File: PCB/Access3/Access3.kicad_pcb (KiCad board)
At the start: 2 copper layers, 50 x 26.5 mm, 71 parts, among them J1 USB-C, J2 RFID, J3 INPUTS, J4 Shelly, J5 POWER, J6 DOOR, Q1 NX7002AK, Q2 PMF250XNEX, SW1 ESE13V01D, U1 ESP32-PICO-MINI-02, U2 FT231XQ, U3 G3VM-41GR8, U4 LMR16006XDDCR, U5 LMR16006XDDCR, U6 AA, U7 QR

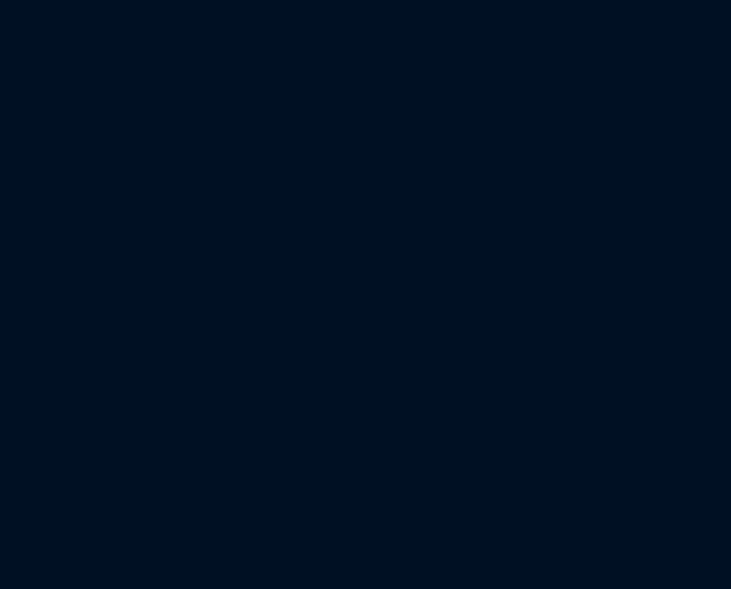
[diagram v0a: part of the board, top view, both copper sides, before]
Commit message: Started new board with two relay outputs
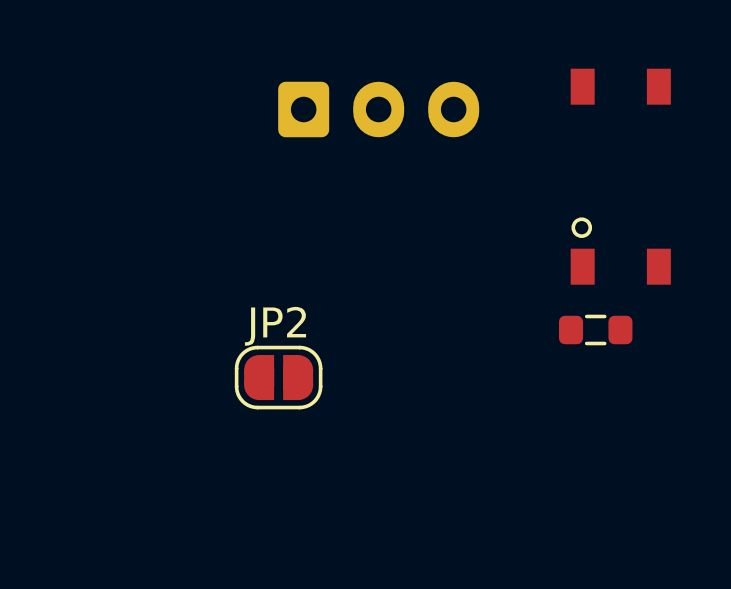
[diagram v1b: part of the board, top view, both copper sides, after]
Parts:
- added J7: DOOR1, RevK:Molex_MiniSPOX_H3RA, F.Cu at (164.1, 67.6)
- added JP2: 12V, Jumper:SolderJumper-2_P1.3mm_Open_RoundedPad1.0x1.5mm, F.Cu at (160.8, 76.5)
- added R25: 1K, RevK:R_0603, F.Cu at (171.3, 75.0)
- added U8: G3VM-41GR8, RevK:Special-SOP-4-3.7x4.55, F.Cu at (172.2, 69.8)
- J6: value DOOR -> DOOR2
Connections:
- R16 pad 2: OUT1 -> RELAY2
- U1 pad 17: unconnected-(U1-Pad17) -> RELAY2
- U1 pad 18: OUT1 -> RELAY1
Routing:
- net RELAY2: track 0.00 -> 32.2 mm, vias 0 -> 2
- net OUT1: track 32.2 -> 0.00 mm, vias 2 -> 0
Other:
- board text added: "Solar System Access3"
- board text removed: "Solar System Access2"

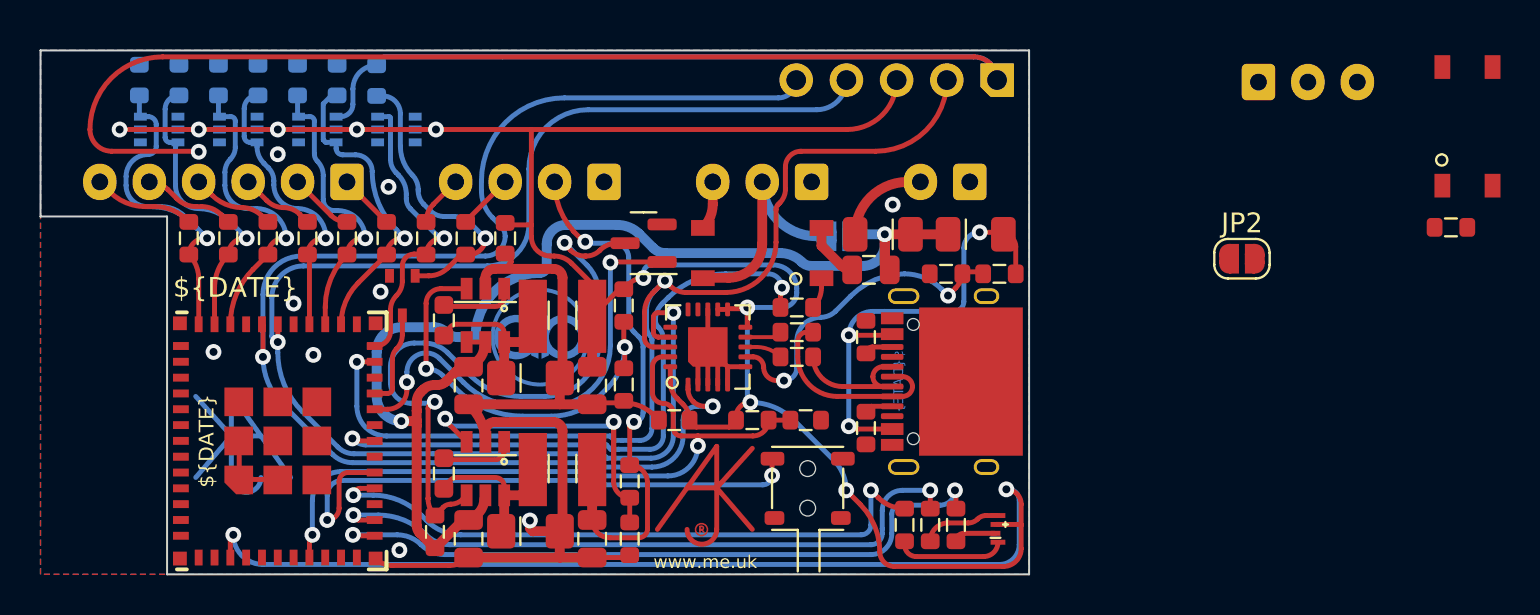
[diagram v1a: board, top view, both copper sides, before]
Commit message: New dual output board
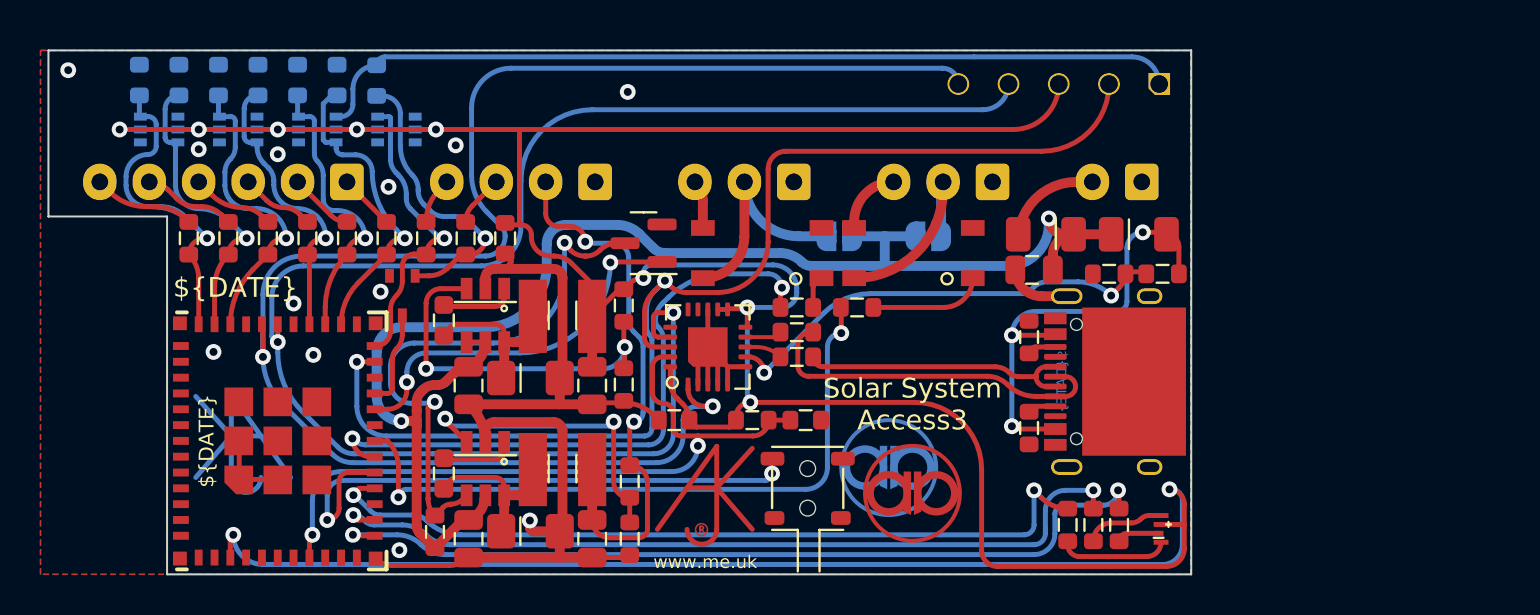
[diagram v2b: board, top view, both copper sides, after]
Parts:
- added U9: AA, RevK:AA, F.Cu at (144.1, 88.4)
- JP2: moved to B.Cu
- moved R25 30.3 mm to (141.3, 79.0), turned to 180 degrees
- moved U8 28.7 mm to (144.2, 76.2), turned to 90 degrees
- moved J7 19.1 mm to (145.7, 72.7), turned to 180 degrees
- moved U6 18.8 mm to (142.9, 87.1)
- moved JP2 15.9 mm to (144.9, 75.4)
- moved J5 8.70 mm to (154.4, 72.7)
- moved C17 8.25 mm to (150.2, 77.1)
- moved D5 8.25 mm to (156.6, 90.2)
- moved D8 8.25 mm to (155.6, 75.3)
- moved D9 8.25 mm to (150.8, 75.3)
- moved J1 8.25 mm to (153.8, 82.8)
- moved R17 8.25 mm to (154.6, 90.0)
- moved R18 8.25 mm to (151.9, 90.0)
- moved R19 8.25 mm to (153.2, 90.0)
- moved R2 8.25 mm to (156.8, 77.3)
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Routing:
- net GND: track 122.2 -> 75.0 mm, vias 10 -> 12
- net RELAY1: track 0.00 -> 34.5 mm, vias 0 -> 2
- net +3.3V: track 158.8 -> 182.6 mm, vias 11 -> 10
- net O: track 70.0 -> 81.1 mm
- net +12V: track 59.4 -> 69.4 mm
- net Net-(J7-Pad2): track 0.00 -> 9.54 mm
- net G: track 32.0 -> 40.3 mm
- net B: track 33.7 -> 42.0 mm
- net R: track 35.0 -> 43.2 mm
- net BOOT: track 53.6 -> 61.7 mm
- net Net-(J1-PadA7): track 10.2 -> 18.2 mm
- net I: track 72.7 -> 80.3 mm
- net Net-(J1-PadA6): track 6.80 -> 13.7 mm
- net Net-(Q1-Pad3): track 34.2 -> 27.5 mm
- net Net-(R2-Pad2): track 16.7 -> 23.1 mm
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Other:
- board size 50 x 26.5 mm -> 57.8 x 26.5 mm
- board text added: "Lock Relays"

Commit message: New cases
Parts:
- moved U6 2.48 mm to (144.5, 85.2)
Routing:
- net GND: track 75.0 -> 76.7 mm, vias 12 -> 14
- net SHDN: track 18.9 -> 20.5 mm
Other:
- board text added: "1"
- board text added: "2"
- board text added: "DC"
- board text added: "GPIO 1-6"
- board text removed: "Inputs 1-6"
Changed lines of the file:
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@@
   (footprint "RevK:D_1206_" (layer "F.Cu")
     (at 124.78 82.57)
-    (property "JLCPCB Rotation Offset" "180")
+    (property "JLCPCB Rotation Offset" "0")
     (property "LCSC Part #" "C143805")
     (property "Manufacturer" "Bourns")
@@
   (footprint "RevK:D_1206_" (layer "F.Cu")
     (at 124.77 90.31)
-    (property "JLCPCB Rotation Offset" "180")
+    (property "JLCPCB Rotation Offset" "0")
     (property "LCSC Part #" "C143805")
     (property "Manufacturer" "Bourns")
@@
     (descr "SOT-323, SC-70")
     (tags "SOT-323 SC-70")
-    (property "JLCPCB Rotation Offset" "180")
+    (property "JLCPCB Rotation Offset" "0")
     (property "LCSC Part #" "C504047")
     (property "Part No" "PMF250XNEX")
@@
   )
   (footprint "RevK:AA" (layer "B.Cu")
-    (at 142.9 87.1 180)
+    (at 144.5 85.2 180)
     (property "Note" "Non part, PCB printed")
     (property "Sheetfile" "Access3.kicad_sch")
@@
     )
   )
-  (gr_line (start 135.6 71.1) (end 135.6 70.5) (layer "B.SilkS") (width 0.15))
-  (gr_line (start 133.1 70.5) (end 135.6 70.5) (layer "B.SilkS") (width 0.15))
-  (gr_line (start 133.1 70.5) (end 133.1 71.1) (layer "B.SilkS") (width 0.15))
+  (gr_line (start 142.7 76.9) (end 153.2 76.9) (layer "B.SilkS") (width 0.12))
+  (gr_line (start 135 70.4) (end 133.8 70.1) (layer "B.SilkS") (width 0.15))
+  (gr_line (start 145 70.4) (end 143.8 70.1) (layer "B.SilkS") (width 0.15))
   (gr_line (start 143.1 70.4) (end 143.1 71) (layer "B.SilkS") (width 0.15))
-  (gr_line (start 143.1 70.4) (end 145.6 70.4) (layer "B.SilkS") (width 0.15))
+  (gr_line (start 135.6 71) (end 135.6 70.4) (layer "B.SilkS") (width 0.15))
+  (gr_line (start 133.1 70.4) (end 133.1 71) (layer "B.SilkS") (width 0.15))
+  (gr_line (start 143.1 70.4) (end 143.7 70.4) (layer "B.SilkS") (width 0.15))
+  (gr_line (start 135 70.4) (end 135.6 70.4) (layer "B.SilkS") (width 0.15))
   (gr_line (start 145.7 73.7) (end 145.7 74.2) (layer "B.SilkS") (width 0.12))
+  (gr_line (start 145 70.4) (end 145.6 70.4) (layer "B.SilkS") (width 0.15))
   (gr_line (start 135.6 73.7) (end 135.6 75.4) (layer "B.SilkS") (width 0.12))
+  (gr_line (start 133.1 70.4) (end 133.7 70.4) (layer "B.SilkS") (width 0.15))
+  (gr_line (start 142.7 76.3) (end 142.7 76.9) (layer "B.SilkS") (width 0.12))
   (gr_line (start 138.8 75.4) (end 135.6 75.4) (layer "B.SilkS") (width 0.12))
+  (gr_line (start 153.2 76.9) (end 153.2 74.1) (layer "B.SilkS") (width 0.12))
   (gr_line (start 145.6 71) (end 145.6 70.4) (layer "B.SilkS") (width 0.15))
   (gr_line (start 100.4 66) (end 158.2 66) (layer "Edge.Cuts") (width 0.1))
@@
     (effects (font (size 0.8 0.8) (thickness 0.1)) (justify mirror))
   )
-  (gr_text "Power" (at 153.9 74.575) (layer "B.SilkS")
-    (effects (font (size 0.8 0.8) (thickness 0.1)) (justify mirror))
-  )
   (gr_text "Solar System\nAccess3" (at 123.5 87.4) (layer "B.SilkS")
     (effects (font (size 1 1) (thickness 0.15)) (justify mirror))
   )
+  (gr_text "DC" (at 154.4 74.6) (layer "B.SilkS")
+    (effects (font (size 0.8 0.8) (thickness 0.1)) (justify mirror))
+  )
+  (gr_text "1" (at 144.4 71.35) (layer "B.SilkS")
+    (effects (font (size 0.8 0.8) (thickness 0.1)) (justify mirror))
+  )
+  (gr_text "2" (at 134.35 71.35) (layer "B.SilkS")
+    (effects (font (size 0.8 0.8) (thickness 0.1)) (justify mirror))
+  )
   (gr_text "⏚" (at 148.1 70.4 180) (layer "B.SilkS")
     (effects (font (size 1 1) (thickness 0.15)) (justify mirror))
@@
     (effects (font (size 1 1) (thickness 0.15)) (justify mirror))
   )
-  (gr_text "Inputs 1-6" (at 101 70 90) (layer "B.SilkS")
+  (gr_text "GPIO 1-6" (at 110.5 74.4) (layer "B.SilkS")
     (effects (font (size 0.8 0.8) (thickness 0.1)) (justify mirror))
   )
@@
   (segment (start 133.75 82.9) (end 133.75 81) (width 0.25) (layer "F.Cu") (net 3))
   (segment (start 110.05 87.7) (end 110.05 85.75) (width 0.25) (layer "F.Cu") (net 3))
+  (segment (start 125.03 82.57) (end 124.7 82.9) (width 0.5) (layer "F.Cu") (net 3))
   (segment (start 133.25 82.9) (end 133.25 81.5) (width 0.25) (layer "F.Cu") (net 3))
   (segment (start 110.05 87.7) (end 112 87.7) (width 0.25) (layer "F.Cu") (net 3))
   (segment (start 133.75 79.1) (end 133.75 81) (width 0.25) (layer "F.Cu") (net 3))
   (segment (start 134.75 82.9) (end 134.75 82) (width 0.25) (layer "F.Cu") (net 3))
+  (segment (start 126.2625 82.57) (end 125.03 82.57) (width 0.5) (layer "F.Cu") (net 3))
   (segment (start 123.8 76.375) (end 123.8 76.7) (width 0.25) (layer "F.Cu") (net 3))
   (via (at 108.75 81.25) (size 0.8) (drill 0.4) (layers "F.Cu" "B.Cu") (free) (net 3))
@@
   (via (at 117.2 78.2) (size 0.8) (drill 0.4) (layers "F.Cu" "B.Cu") (free) (net 3))
   (via (at 112 71.25) (size 0.8) (drill 0.4) (layers "F.Cu" "B.Cu") (net 3))
+  (via (at 124.7 82.9) (size 0.8) (drill 0.4) (layers "F.Cu" "B.Cu") (net 3))
   (via (at 112.8 78.8) (size 0.8) (drill 0.4) (layers "F.Cu" "B.Cu") (free) (net 3))
   (via (at 124.75 89.7755) (size 0.8) (drill 0.4) (layers "F.Cu" "B.Cu") (net 3))
-  (via (at 121 70.8) (size 0.8) (drill 0.4) (layers "F.Cu" "B.Cu") (free) (net 3))
+  (via (at 126.4 80.3) (size 0.8) (drill 0.4) (layers "F.Cu" "B.Cu") (net 3))
+  (via (at 121 71.1) (size 0.8) (drill 0.4) (layers "F.Cu" "B.Cu") (free) (net 3))
   (arc (start 120.684315 92.05) (mid 121.20694 91.946043) (end 121.65 91.65) (width 0.25) (layer "F.Cu") (net 3))
   (arc (start 123.8 76.7) (mid 123.770711 76.770711) (end 123.7 76.8) (width 0.25) (layer "F.Cu") (net 3))
@@
   (via (at 118.529927 82.779927) (size 0.8) (drill 0.4) (layers "F.Cu" "B.Cu") (net 10))
   (arc (start 118.529927 83.170073) (mid 118.242913 83.862986) (end 117.55 84.15) (width 0.25) (layer "F.Cu") (net 10))
-  (segment (start 119.5 81.3) (end 124.249198 81.3) (width 0.25) (layer "B.Cu") (net 10))
-  (segment (start 118.529927 82.270073) (end 118.529927 82.779927) (width 0.25) (layer "B.Cu") (net 10))
-  (arc (start 124.249198 81.3) (mid 127.483335 79.960376) (end 128.822959 76.726239) (width 0.25) (layer "B.Cu") (net 10))
-  (arc (start 119.5 81.3) (mid 118.814055 81.584128) (end 118.529927 82.270073) (width 0.25) (layer "B.Cu") (net 10))
+  (segment (start 118.529927 82.779927) (end 118.529927 82.270073) (width 0.25) (layer "B.Cu") (net 10))
+  (segment (start 128.822959 76.726239) (end 128.822959 80.077041) (width 0.25) (layer "B.Cu") (net 10))
+  (segment (start 119.5 81.3) (end 127.6 81.3) (width 0.25) (layer "B.Cu") (net 10))
+  (arc (start 118.529927 82.270073) (mid 118.814055 81.584128) (end 119.5 81.3) (width 0.25) (layer "B.Cu") (net 10))
+  (arc (start 128.822959 80.077041) (mid 128.464763 80.941804) (end 127.6 81.3) (width 0.25) (layer "B.Cu") (net 10))
   (segment (start 111.25 81.5) (end 111.25 79.9) (width 0.25) (layer "F.Cu") (net 11))
   (segment (start 132.75 83.146447) (end 132.75 82.9375) (width 0.25) (layer "F.Cu") (net 11))

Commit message: PSTM connectors
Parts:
- J2: footprint RevK:Molex_MiniSPOX_H4RA -> RevK:PTSM-HH-4-RA
- J3: footprint RevK:Molex_MiniSPOX_H6RA -> RevK:PTSM-HH-6-RA
- J5: footprint RevK:Molex_MiniSPOX_H2RA -> RevK:PTSM-HH-2-RA
- J6, J7: footprint RevK:Molex_MiniSPOX_H3RA -> RevK:PTSM-HH-3-RA
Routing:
- net IO6: track 18.8 -> 16.2 mm
- net Net-(J3-Pad6): track 4.22 -> 5.08 mm
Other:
- board size 57.8 x 26.5 mm -> 57.8 x 27 mm

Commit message: White socket
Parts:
- J6: footprint RevK:PTSM-HH-3-RA -> RevK:PTSM-HH-3-RA-W
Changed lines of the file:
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@@
     )
   )
-  (footprint "RevK:PTSM-HH-3-RA" (layer "F.Cu")
+  (footprint "RevK:PTSM-HH-3-RA-W" (layer "F.Cu")
     (at 135.6 72.7 180)
     (property "Sheetfile" "Access3.kicad_sch")
@@
       (effects (font (size 1 1) (thickness 0.15)))
     )
+    (fp_line (start -4.45 7.05) (end -4.45 6.05) (layer "F.SilkS") (width 0.12))
     (fp_line (start -4.45 7.05) (end 4.45 7.05) (layer "F.SilkS") (width 0.12))
-    (fp_line (start -4.45 7.05) (end -4.45 6.05) (layer "F.SilkS") (width 0.12))
     (fp_line (start 4.45 7.05) (end 4.45 6.05) (layer "F.SilkS") (width 0.12))
+    (fp_line (start -4.6 17.75) (end -4.6 -0.3) (layer "F.CrtYd") (width 0.12))
     (fp_line (start -4.6 -0.3) (end 4.6 -0.3) (layer "F.CrtYd") (width 0.12))
+    (fp_line (start 4.6 17.75) (end -4.6 17.75) (layer "F.CrtYd") (width 0.12))
     (fp_line (start 4.6 -0.3) (end 4.6 17.75) (layer "F.CrtYd") (width 0.12))
-    (fp_line (start 4.6 17.75) (end -4.6 17.75) (layer "F.CrtYd") (width 0.12))
-    (fp_line (start -4.6 17.75) (end -4.6 -0.3) (layer "F.CrtYd") (width 0.12))
-    (fp_line (start -4.6 -0.3) (end 4.6 -0.3) (layer "F.Fab") (width 0.12))
     (fp_line (start 4.6 7.2) (end -4.6 7.2) (layer "F.Fab") (width 0.12))
     (fp_line (start -4.6 7.2) (end -4.6 -0.3) (layer "F.Fab") (width 0.12))
     (fp_line (start 4.6 -0.3) (end 4.6 7.2) (layer "F.Fab") (width 0.12))
+    (fp_line (start -4.6 -0.3) (end 4.6 -0.3) (layer "F.Fab") (width 0.12))
     (pad "1" thru_hole roundrect (at -2.5 0 180) (size 1.7 1.85) (drill 0.85) (layers *.Cu *.Mask) (roundrect_rratio 0.25)
       (net 3 "GND") (pinfunction "Pin_1") (pintype "passive"))
@@
     (pad "3" thru_hole oval (at 2.5 0 180) (size 1.7 1.85) (drill 0.85) (layers *.Cu *.Mask)
       (net 41 "Net-(J6-Pad3)") (pinfunction "Pin_3") (pintype "passive"))
-    (model "${REVK_3D}/pxc_1778638_03_PTSM-0-5-3-HH-2-5-THR-R32_3D.stp"
+    (model "${REVK_3D}/pxc_1814854_02_PTSM-0-5-3-HH-2-5-THR-WH-R32_3D.stp"
       (offset (xyz 4.6 -7.2 0))
       (scale (xyz 1 1 1))

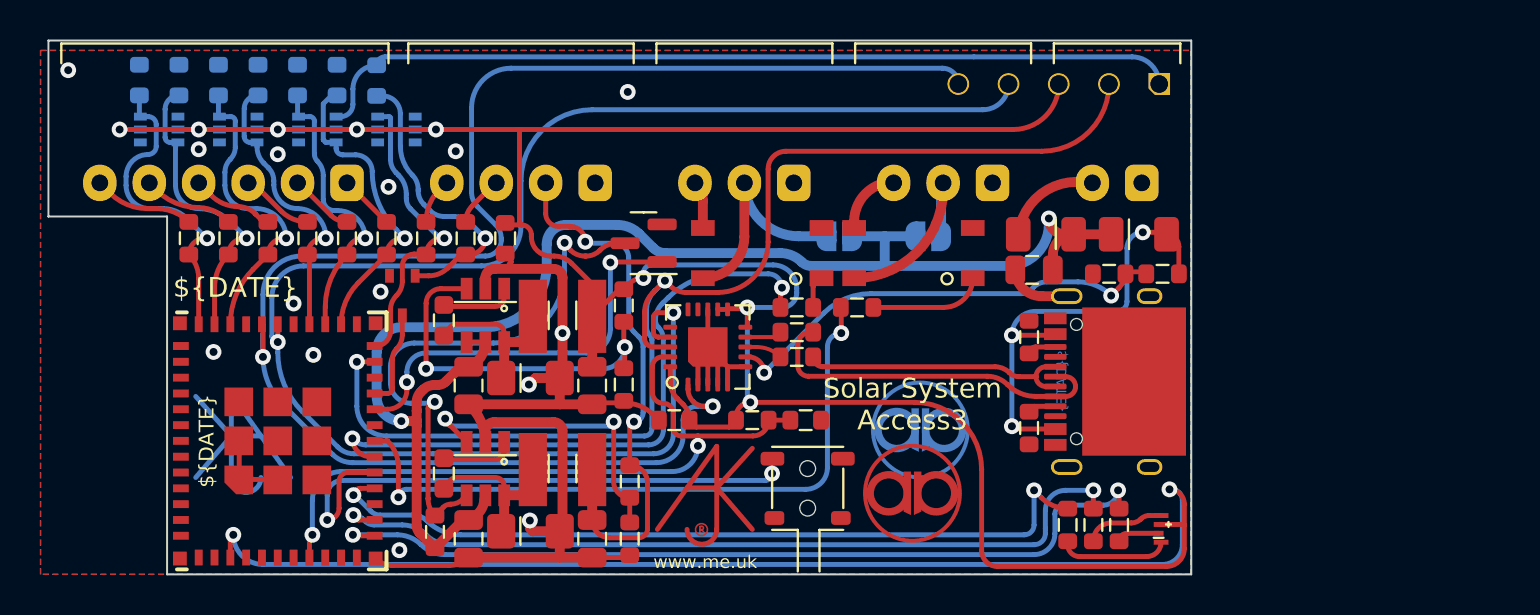
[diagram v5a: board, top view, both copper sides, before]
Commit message: Updated for locking smaller sockets
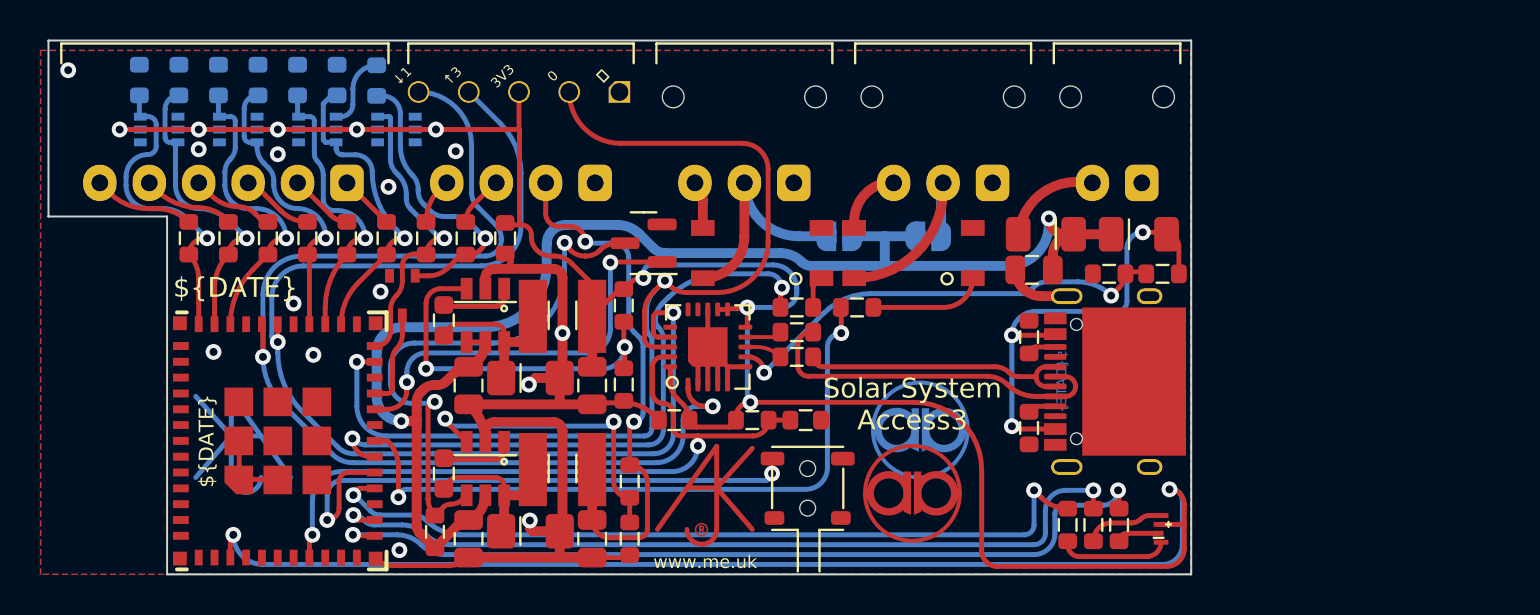
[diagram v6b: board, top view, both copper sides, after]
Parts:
- J4: moved to F.Cu
- J5: footprint RevK:PTSM-HH-2-RA -> RevK:PTSM-HH1-2-RA
- J6: footprint RevK:PTSM-HH-3-RA-W -> RevK:PTSM-HH1-3-RA-W
- J7: footprint RevK:PTSM-HH-3-RA -> RevK:PTSM-HH1-3-RA
- moved J4 27.3 mm to (124.2, 68.1)
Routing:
- net GND: track 76.7 -> 36.2 mm, vias 14 -> 13
- net +3.3V: track 182.6 -> 156.0 mm
- net O: track 81.0 -> 57.1 mm
- net I: track 80.3 -> 58.5 mm
- net BOOT: track 61.7 -> 54.3 mm
- net Net-(J3-Pad5): track 4.58 -> 3.82 mm
- net Net-(J3-Pad6): track 5.08 -> 4.34 mm
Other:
- board text removed: "Lock Relays"
